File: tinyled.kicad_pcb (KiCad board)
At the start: 2 copper layers, 30.1 x 14 mm, 50 parts, among them J1 Conn_01x01_Female, J10 Conn_01x01_Female, J11 Conn_01x01_Female, J12 Conn_01x01_Female, J13 Conn_01x01_Female, J14 Conn_01x01_Female, J15 Conn_01x01_Female, J16 Conn_01x01_Female, J17 Conn_01x01_Female, J18 Conn_01x01_Female, J19 Conn_01x01_Female, J2 Conn_01x01_Female, J20 Conn_01x01_Female, J3 Conn_01x01_Female, J4 Conn_01x01_Female, J5 Conn_01x01_Female, J6 Conn_01x01_Female, J7 Conn_01x01_Female, J8 Conn_01x01_Female, J9 Conn_01x01_Female

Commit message: update
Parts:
- removed the D1 at (7.80, 84.0)
- removed the D1 at (1.80, 84.0)
- removed the D1 at (-4.20, 84.0)
- removed the D1 at (-10.2, 84.0)
- removed the R1 at (7.80, 88.4)
- removed the R1 at (1.80, 88.4)
- removed the R1 at (-4.20, 88.4)
- removed the R1 at (-10.2, 88.4)
- moved J1 101.5 mm to (-16.2, 78.9)
- moved J4 101.1 mm to (-16.2, 93.5)
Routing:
- net +3V3: track 0.00 -> 4.12 mm
- net GND: track 0.00 -> 4.10 mm
- net Net-(D1-Pad1): track 0.00 -> 2.34 mm
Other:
- board size 30.1 x 14 mm -> 30.1 x 20.3 mm

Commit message: send first version to fab
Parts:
- removed the D1 at (76.1, 103.0)
- removed D10, D2, D3, D4, D5, D6, D7, D8, D9: LED, Diode_SMD:D_0805_2012Metric_Pad1.15x1.40mm_HandSolder
- removed J10, J11, J12, J13, J14, J15, J16, J17, J18, J19, J2, J20, J3, J5, J6, J7, J8, J9: Conn_01x01_Female, Wickerlib:CONN-HEADER-STRAIGHT-P2.54MM-1x01
- removed the R1 at (76.1, 109.7)
- removed R10, R2, R3, R4, R5, R6, R7, R8, R9: R, Resistor_SMD:R_0805_2012Metric_Pad1.15x1.40mm_HandSolder
- added D1: LED, Diode_SMD:D_0805_2012Metric_Pad1.15x1.40mm_HandSolder, F.Cu at (23.8, 84.0)
- added D1: LED, Diode_SMD:D_0805_2012Metric_Pad1.15x1.40mm_HandSolder, F.Cu at (13.8, 84.0)
- added D1: LED, Diode_SMD:D_0805_2012Metric_Pad1.15x1.40mm_HandSolder, F.Cu at (3.80, 84.0)
- added D1: LED, Diode_SMD:D_0805_2012Metric_Pad1.15x1.40mm_HandSolder, F.Cu at (-6.20, 84.0)
- added J1: Conn_01x01_Female, Wickerlib:CONN-HEADER-STRAIGHT-P2.54MM-1x01, F.Cu at (23.8, 78.9)
- added J1: Conn_01x01_Female, Wickerlib:CONN-HEADER-STRAIGHT-P2.54MM-1x01, F.Cu at (13.8, 78.9)
- added J1: Conn_01x01_Female, Wickerlib:CONN-HEADER-STRAIGHT-P2.54MM-1x01, F.Cu at (3.78, 78.9)
- added J1: Conn_01x01_Female, Wickerlib:CONN-HEADER-STRAIGHT-P2.54MM-1x01, F.Cu at (-6.22, 78.9)
- added J4: Conn_01x01_Female, Wickerlib:CONN-HEADER-STRAIGHT-P2.54MM-1x01, F.Cu at (23.8, 93.5)
- added J4: Conn_01x01_Female, Wickerlib:CONN-HEADER-STRAIGHT-P2.54MM-1x01, F.Cu at (13.8, 93.5)
- added J4: Conn_01x01_Female, Wickerlib:CONN-HEADER-STRAIGHT-P2.54MM-1x01, F.Cu at (3.80, 93.5)
- added J4: Conn_01x01_Female, Wickerlib:CONN-HEADER-STRAIGHT-P2.54MM-1x01, F.Cu at (-6.20, 93.5)
- added R1: R, Resistor_SMD:R_0805_2012Metric_Pad1.15x1.40mm_HandSolder, F.Cu at (23.8, 88.4)
- added R1: R, Resistor_SMD:R_0805_2012Metric_Pad1.15x1.40mm_HandSolder, F.Cu at (13.8, 88.4)
- added R1: R, Resistor_SMD:R_0805_2012Metric_Pad1.15x1.40mm_HandSolder, F.Cu at (3.80, 88.4)
- added R1: R, Resistor_SMD:R_0805_2012Metric_Pad1.15x1.40mm_HandSolder, F.Cu at (-6.20, 88.4)
- added V: HOLE-PLATED-200MIL, Wickerlib:HOLE-UNPLATED-200MIL, F.Cu at (16.8, 75.0)
- added V: HOLE-PLATED-200MIL, Wickerlib:HOLE-UNPLATED-200MIL, F.Cu at (18.7, 94.5)
- added V: HOLE-PLATED-200MIL, Wickerlib:HOLE-UNPLATED-200MIL, F.Cu at (8.72, 94.5)
- added V: HOLE-PLATED-200MIL, Wickerlib:HOLE-UNPLATED-200MIL, F.Cu at (-1.28, 94.5)
- added V: HOLE-PLATED-200MIL, Wickerlib:HOLE-UNPLATED-200MIL, F.Cu at (17.7, 75.0)
- added V: HOLE-PLATED-200MIL, Wickerlib:HOLE-UNPLATED-200MIL, F.Cu at (7.75, 75.0)
- added V: HOLE-PLATED-200MIL, Wickerlib:HOLE-UNPLATED-200MIL, F.Cu at (-2.25, 75.0)
- added V: HOLE-PLATED-200MIL, Wickerlib:HOLE-UNPLATED-200MIL, F.Cu at (17.8, 94.6)
- added V: HOLE-PLATED-200MIL, Wickerlib:HOLE-UNPLATED-200MIL, F.Cu at (7.80, 94.6)
- added V: HOLE-PLATED-200MIL, Wickerlib:HOLE-UNPLATED-200MIL, F.Cu at (-2.20, 94.6)
- added V: HOLE-PLATED-200MIL, Wickerlib:HOLE-UNPLATED-200MIL, F.Cu at (-13.1, 94.6)
- added V: HOLE-PLATED-200MIL, Wickerlib:HOLE-UNPLATED-200MIL, F.Cu at (6.84, 75.0)
- added V: HOLE-PLATED-200MIL, Wickerlib:HOLE-UNPLATED-200MIL, F.Cu at (-11.3, 94.5)
- added V: HOLE-PLATED-200MIL, Wickerlib:HOLE-UNPLATED-200MIL, F.Cu at (-12.2, 94.6)
- added V: HOLE-PLATED-200MIL, Wickerlib:HOLE-UNPLATED-200MIL, F.Cu at (-11.3, 75.0)
- added V: HOLE-PLATED-200MIL, Wickerlib:HOLE-UNPLATED-200MIL, F.Cu at (-13.2, 75.0)
- added V: HOLE-PLATED-200MIL, Wickerlib:HOLE-UNPLATED-200MIL, F.Cu at (-12.3, 75.0)
- added V: HOLE-PLATED-200MIL, Wickerlib:HOLE-UNPLATED-200MIL, F.Cu at (-3.16, 75.0)
- added V: HOLE-PLATED-200MIL, Wickerlib:HOLE-UNPLATED-200MIL, F.Cu at (18.7, 75.0)
- added V: HOLE-PLATED-200MIL, Wickerlib:HOLE-UNPLATED-200MIL, F.Cu at (8.67, 75.0)
- added V: HOLE-PLATED-200MIL, Wickerlib:HOLE-UNPLATED-200MIL, F.Cu at (-1.33, 75.0)
- added V: HOLE-PLATED-200MIL, Wickerlib:HOLE-UNPLATED-200MIL, F.Cu at (16.9, 94.6)
- added V: HOLE-PLATED-200MIL, Wickerlib:HOLE-UNPLATED-200MIL, F.Cu at (6.88, 94.6)
- added V: HOLE-PLATED-200MIL, Wickerlib:HOLE-UNPLATED-200MIL, F.Cu at (-3.12, 94.6)
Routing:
- net +3V3: track 4.12 -> 20.6 mm
- net GND: track 4.10 -> 20.5 mm
- net Net-(D1-Pad1): track 2.34 -> 11.7 mm
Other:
- board size 30.1 x 20.3 mm -> 48.8 x 20.6 mm

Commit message: rev2
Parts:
- removed the D1 at (23.8, 84.0)
- removed the D1 at (13.8, 84.0)
- removed the D1 at (3.80, 84.0)
- removed the D1 at (-6.20, 84.0)
- removed the J1 at (23.8, 78.9)
- removed the J1 at (13.8, 78.9)
- removed the J1 at (3.78, 78.9)
- removed the J1 at (-6.22, 78.9)
- removed the J4 at (23.8, 93.5)
- removed the J4 at (13.8, 93.5)
- removed the J4 at (3.80, 93.5)
- removed the J4 at (-6.20, 93.5)
- removed the R1 at (23.8, 88.4)
- removed the R1 at (13.8, 88.4)
- removed the R1 at (3.80, 88.4)
- removed the R1 at (-6.20, 88.4)
- removed the V at (16.8, 75.0)
- removed the V at (18.7, 94.5)
- removed the V at (8.72, 94.5)
- removed the V at (-1.28, 94.5)
- removed the V at (17.7, 75.0)
- removed the V at (7.75, 75.0)
- removed the V at (-2.25, 75.0)
- removed the V at (17.8, 94.6)
- removed the V at (7.80, 94.6)
- removed the V at (-2.20, 94.6)
- removed the V at (-13.1, 94.6)
- removed the V at (6.84, 75.0)
- removed the V at (-11.3, 94.5)
- removed the V at (-12.2, 94.6)
- removed the V at (-3.16, 75.0)
- removed the V at (18.7, 75.0)
- removed the V at (8.67, 75.0)
- removed the V at (-1.33, 75.0)
- removed the V at (16.9, 94.6)
- removed the V at (6.88, 94.6)
- removed the V at (-3.12, 94.6)
- added D1: LED, Diode_SMD:D_0805_2012Metric_Pad1.15x1.40mm_HandSolder, B.Cu at (-16.2, 84.0)
- added D1: LED, Diode_SMD:D_0805_2012Metric_Pad1.15x1.40mm_HandSolder, F.Cu at (11.8, 84.0)
- added D1: LED, Diode_SMD:D_0805_2012Metric_Pad1.15x1.40mm_HandSolder, B.Cu at (-2.19, 84.0)
- added D1: LED, Diode_SMD:D_0805_2012Metric_Pad1.15x1.40mm_HandSolder, B.Cu at (-9.19, 84.0)
- added D1: LED, Diode_SMD:D_0805_2012Metric_Pad1.15x1.40mm_HandSolder, B.Cu at (4.81, 84.0)
- added D1: LED, Diode_SMD:D_0805_2012Metric_Pad1.15x1.40mm_HandSolder, B.Cu at (11.8, 84.0)
- added D1: LED, Diode_SMD:D_0805_2012Metric_Pad1.15x1.40mm_HandSolder, F.Cu at (-9.20, 84.0)
- added D1: LED, Diode_SMD:D_0805_2012Metric_Pad1.15x1.40mm_HandSolder, F.Cu at (-2.20, 84.0)
- added D1: LED, Diode_SMD:D_0805_2012Metric_Pad1.15x1.40mm_HandSolder, F.Cu at (4.80, 84.0)
- added J1: Conn_01x01_Female, Wickerlib:CONN-HEADER-STRAIGHT-P2.54MM-1x01, F.Cu at (-9.22, 78.9)
- added J1: Conn_01x01_Female, Wickerlib:CONN-HEADER-STRAIGHT-P2.54MM-1x01, F.Cu at (-2.22, 78.9)
- added J1: Conn_01x01_Female, Wickerlib:CONN-HEADER-STRAIGHT-P2.54MM-1x01, F.Cu at (4.78, 78.9)
- added J1: Conn_01x01_Female, Wickerlib:CONN-HEADER-STRAIGHT-P2.54MM-1x01, F.Cu at (11.8, 78.9)
- added J4: Conn_01x01_Female, Wickerlib:CONN-HEADER-STRAIGHT-P2.54MM-1x01, F.Cu at (-9.20, 93.5)
- added J4: Conn_01x01_Female, Wickerlib:CONN-HEADER-STRAIGHT-P2.54MM-1x01, F.Cu at (-2.20, 93.5)
- added J4: Conn_01x01_Female, Wickerlib:CONN-HEADER-STRAIGHT-P2.54MM-1x01, F.Cu at (4.80, 93.5)
- added J4: Conn_01x01_Female, Wickerlib:CONN-HEADER-STRAIGHT-P2.54MM-1x01, F.Cu at (11.8, 93.5)
- added R1: R, Resistor_SMD:R_0805_2012Metric_Pad1.15x1.40mm_HandSolder, B.Cu at (-2.19, 88.4)
- added R1: R, Resistor_SMD:R_0805_2012Metric_Pad1.15x1.40mm_HandSolder, F.Cu at (11.8, 88.4)
- added R1: R, Resistor_SMD:R_0805_2012Metric_Pad1.15x1.40mm_HandSolder, B.Cu at (-16.2, 88.4)
- added R1: R, Resistor_SMD:R_0805_2012Metric_Pad1.15x1.40mm_HandSolder, B.Cu at (-9.19, 88.4)
- added R1: R, Resistor_SMD:R_0805_2012Metric_Pad1.15x1.40mm_HandSolder, B.Cu at (4.81, 88.4)
- added R1: R, Resistor_SMD:R_0805_2012Metric_Pad1.15x1.40mm_HandSolder, B.Cu at (11.8, 88.4)
- added R1: R, Resistor_SMD:R_0805_2012Metric_Pad1.15x1.40mm_HandSolder, F.Cu at (-9.20, 88.4)
- added R1: R, Resistor_SMD:R_0805_2012Metric_Pad1.15x1.40mm_HandSolder, F.Cu at (-2.20, 88.4)
- added R1: R, Resistor_SMD:R_0805_2012Metric_Pad1.15x1.40mm_HandSolder, F.Cu at (4.80, 88.4)
- added V: HOLE-PLATED-200MIL, Wickerlib:HOLE-UNPLATED-200MIL, F.Cu at (-0.52, 94.5)
- added V: HOLE-PLATED-200MIL, Wickerlib:HOLE-UNPLATED-200MIL, F.Cu at (-13.7, 94.5)
- added V: HOLE-PLATED-200MIL, Wickerlib:HOLE-UNPLATED-200MIL, F.Cu at (-6.61, 94.5)
- added V: HOLE-PLATED-200MIL, Wickerlib:HOLE-UNPLATED-200MIL, F.Cu at (1.32, 94.5)
- added V: HOLE-PLATED-200MIL, Wickerlib:HOLE-UNPLATED-200MIL, F.Cu at (6.46, 75.0)
- added V: HOLE-PLATED-200MIL, Wickerlib:HOLE-UNPLATED-200MIL, F.Cu at (7.37, 75.0)
- added V: HOLE-PLATED-200MIL, Wickerlib:HOLE-UNPLATED-200MIL, F.Cu at (8.30, 74.9)
- added V: HOLE-PLATED-200MIL, Wickerlib:HOLE-UNPLATED-200MIL, F.Cu at (1.31, 74.9)
- added V: HOLE-PLATED-200MIL, Wickerlib:HOLE-UNPLATED-200MIL, F.Cu at (-0.53, 75.0)
- added V: HOLE-PLATED-200MIL, Wickerlib:HOLE-UNPLATED-200MIL, F.Cu at (0.38, 74.9)
- added V: HOLE-PLATED-200MIL, Wickerlib:HOLE-UNPLATED-200MIL, F.Cu at (-5.70, 74.9)
- added V: HOLE-PLATED-200MIL, Wickerlib:HOLE-UNPLATED-200MIL, F.Cu at (-5.68, 94.5)
- added V: HOLE-PLATED-200MIL, Wickerlib:HOLE-UNPLATED-200MIL, F.Cu at (-7.54, 75.0)
- added V: HOLE-PLATED-200MIL, Wickerlib:HOLE-UNPLATED-200MIL, F.Cu at (-6.62, 75.0)
- added V: HOLE-PLATED-200MIL, Wickerlib:HOLE-UNPLATED-200MIL, F.Cu at (-7.52, 94.5)
- added V: HOLE-PLATED-200MIL, Wickerlib:HOLE-UNPLATED-200MIL, F.Cu at (6.47, 94.5)
- added V: HOLE-PLATED-200MIL, Wickerlib:HOLE-UNPLATED-200MIL, F.Cu at (7.39, 94.5)
- added V: HOLE-PLATED-200MIL, Wickerlib:HOLE-UNPLATED-200MIL, F.Cu at (-12.7, 94.5)
- added V: HOLE-PLATED-200MIL, Wickerlib:HOLE-UNPLATED-200MIL, F.Cu at (0.40, 94.5)
- added V: HOLE-PLATED-200MIL, Wickerlib:HOLE-UNPLATED-200MIL, F.Cu at (8.31, 94.5)
- added V: HOLE-PLATED-200MIL, Wickerlib:HOLE-UNPLATED-200MIL, F.Cu at (-14.6, 94.5)
- moved V 1.42 mm to (-12.7, 75.0)
- moved V 1.42 mm to (-14.6, 75.0)
- moved V 1.42 mm to (-13.7, 75.0)
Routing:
- net Net-(D1-Pad1): track 11.7 -> 23.4 mm
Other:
- board size 48.8 x 20.6 mm -> 33.1 x 20.6 mm

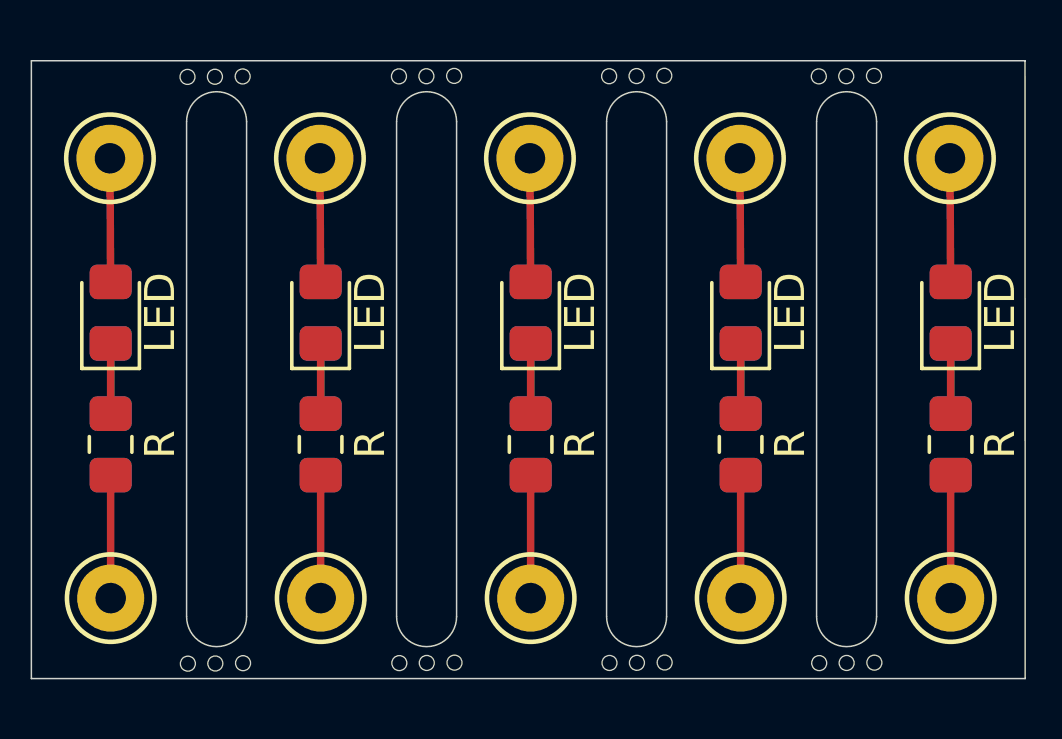
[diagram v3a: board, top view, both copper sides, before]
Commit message: change the mousebites
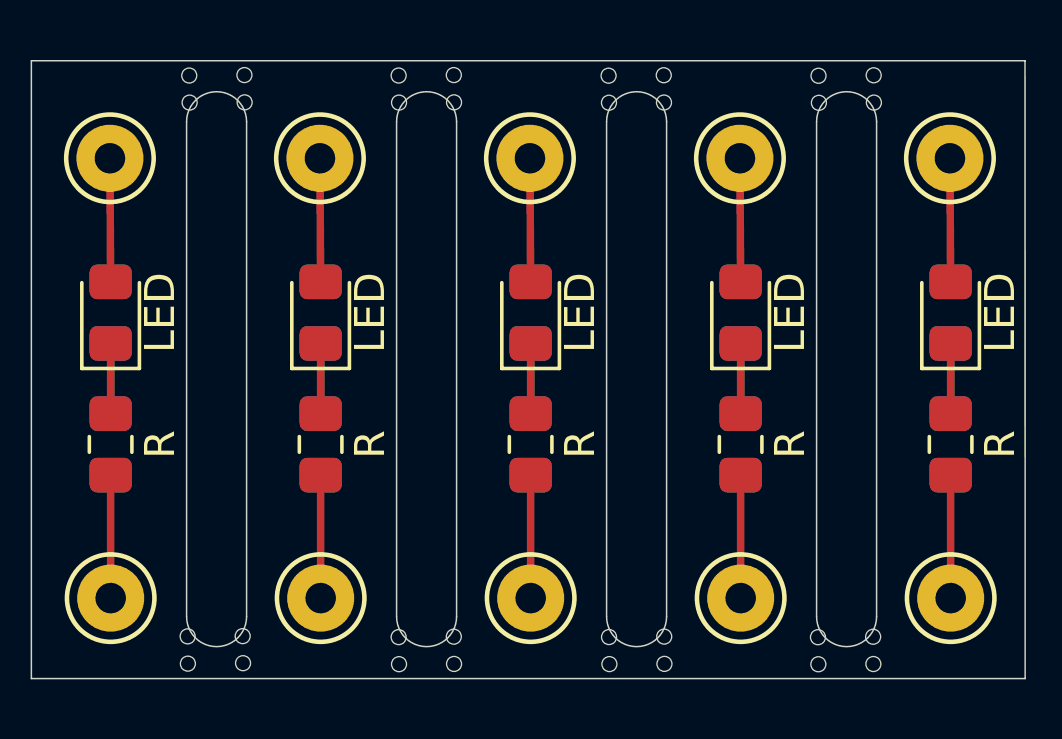
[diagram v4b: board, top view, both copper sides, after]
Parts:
- removed the V at (-0.52, 94.5)
- removed the V at (-6.61, 94.5)
- removed the V at (1.32, 94.5)
- removed the V at (6.46, 75.0)
- removed the V at (7.37, 75.0)
- removed the V at (8.30, 74.9)
- removed the V at (1.31, 74.9)
- removed the V at (-0.53, 75.0)
- removed the V at (0.38, 74.9)
- removed the V at (-5.70, 74.9)
- removed the V at (-5.68, 94.5)
- removed the V at (-7.54, 75.0)
- removed the V at (-6.62, 75.0)
- removed the V at (-12.7, 75.0)
- removed the V at (-14.6, 75.0)
- removed the V at (-13.7, 75.0)
- removed the V at (-7.52, 94.5)
- removed the V at (6.47, 94.5)
- removed the V at (7.39, 94.5)
- removed the V at (0.40, 94.5)
- removed the V at (8.31, 94.5)
- added V: HOLE-PLATED-200MIL, Wickerlib:HOLE-UNPLATED-200MIL, F.Cu at (8.34, 96.9)
- added V: HOLE-PLATED-200MIL, Wickerlib:HOLE-UNPLATED-200MIL, F.Cu at (-5.63, 96.9)
- added V: HOLE-PLATED-200MIL, Wickerlib:HOLE-UNPLATED-200MIL, F.Cu at (-5.65, 96.0)
- added V: HOLE-PLATED-200MIL, Wickerlib:HOLE-UNPLATED-200MIL, F.Cu at (-3.81, 96.0)
- added V: HOLE-PLATED-200MIL, Wickerlib:HOLE-UNPLATED-200MIL, F.Cu at (10.2, 78.2)
- added V: HOLE-PLATED-200MIL, Wickerlib:HOLE-UNPLATED-200MIL, F.Cu at (8.36, 78.2)
- added V: HOLE-PLATED-200MIL, Wickerlib:HOLE-UNPLATED-200MIL, F.Cu at (8.35, 77.3)
- added V: HOLE-PLATED-200MIL, Wickerlib:HOLE-UNPLATED-200MIL, F.Cu at (10.2, 77.3)
- added V: HOLE-PLATED-200MIL, Wickerlib:HOLE-UNPLATED-200MIL, F.Cu at (1.36, 78.2)
- added V: HOLE-PLATED-200MIL, Wickerlib:HOLE-UNPLATED-200MIL, F.Cu at (3.20, 78.2)
- added V: HOLE-PLATED-200MIL, Wickerlib:HOLE-UNPLATED-200MIL, F.Cu at (1.35, 77.3)
- added V: HOLE-PLATED-200MIL, Wickerlib:HOLE-UNPLATED-200MIL, F.Cu at (8.33, 96.0)
- added V: HOLE-PLATED-200MIL, Wickerlib:HOLE-UNPLATED-200MIL, F.Cu at (3.19, 77.3)
- added V: HOLE-PLATED-200MIL, Wickerlib:HOLE-UNPLATED-200MIL, F.Cu at (-5.63, 78.2)
- added V: HOLE-PLATED-200MIL, Wickerlib:HOLE-UNPLATED-200MIL, F.Cu at (-3.80, 78.2)
- added V: HOLE-PLATED-200MIL, Wickerlib:HOLE-UNPLATED-200MIL, F.Cu at (-3.81, 77.3)
- added V: HOLE-PLATED-200MIL, Wickerlib:HOLE-UNPLATED-200MIL, F.Cu at (-5.65, 77.3)
- added V: HOLE-PLATED-200MIL, Wickerlib:HOLE-UNPLATED-200MIL, F.Cu at (-12.6, 78.2)
- added V: HOLE-PLATED-200MIL, Wickerlib:HOLE-UNPLATED-200MIL, F.Cu at (-10.8, 77.3)
- added V: HOLE-PLATED-200MIL, Wickerlib:HOLE-UNPLATED-200MIL, F.Cu at (-12.6, 77.3)
- added V: HOLE-PLATED-200MIL, Wickerlib:HOLE-UNPLATED-200MIL, F.Cu at (-10.8, 78.2)
- added V: HOLE-PLATED-200MIL, Wickerlib:HOLE-UNPLATED-200MIL, F.Cu at (-12.7, 93.6)
- added V: HOLE-PLATED-200MIL, Wickerlib:HOLE-UNPLATED-200MIL, F.Cu at (10.2, 96.0)
- added V: HOLE-PLATED-200MIL, Wickerlib:HOLE-UNPLATED-200MIL, F.Cu at (10.2, 96.9)
- added V: HOLE-PLATED-200MIL, Wickerlib:HOLE-UNPLATED-200MIL, F.Cu at (3.21, 96.0)
- added V: HOLE-PLATED-200MIL, Wickerlib:HOLE-UNPLATED-200MIL, F.Cu at (1.37, 96.0)
- added V: HOLE-PLATED-200MIL, Wickerlib:HOLE-UNPLATED-200MIL, F.Cu at (1.38, 96.9)
- added V: HOLE-PLATED-200MIL, Wickerlib:HOLE-UNPLATED-200MIL, F.Cu at (3.21, 96.9)
- added V: HOLE-PLATED-200MIL, Wickerlib:HOLE-UNPLATED-200MIL, F.Cu at (-3.80, 96.9)
- moved V 1.29 mm to (-14.6, 93.6)
